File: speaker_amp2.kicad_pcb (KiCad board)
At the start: 2 copper layers, 100 x 85 mm, 74 parts, among them J1 Molex_430450227, J2 Molex_430450227, J3 Molex_430450227, J4 Molex_430450227, J5 Molex_1053101106, J6 Molex_430450227, U1 TAS5822MDCPR, U2 TAS5822MDCPR

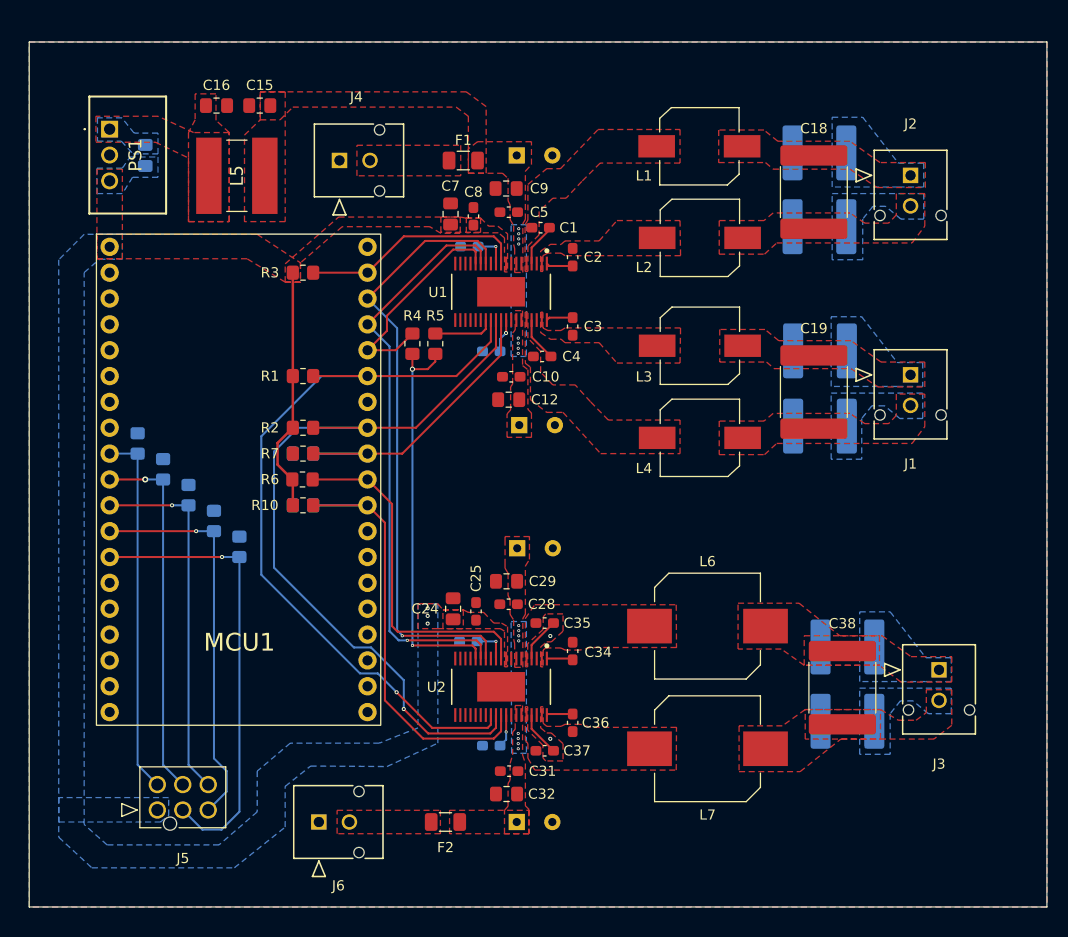
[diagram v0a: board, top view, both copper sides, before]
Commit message: added LEDs and mounting holes
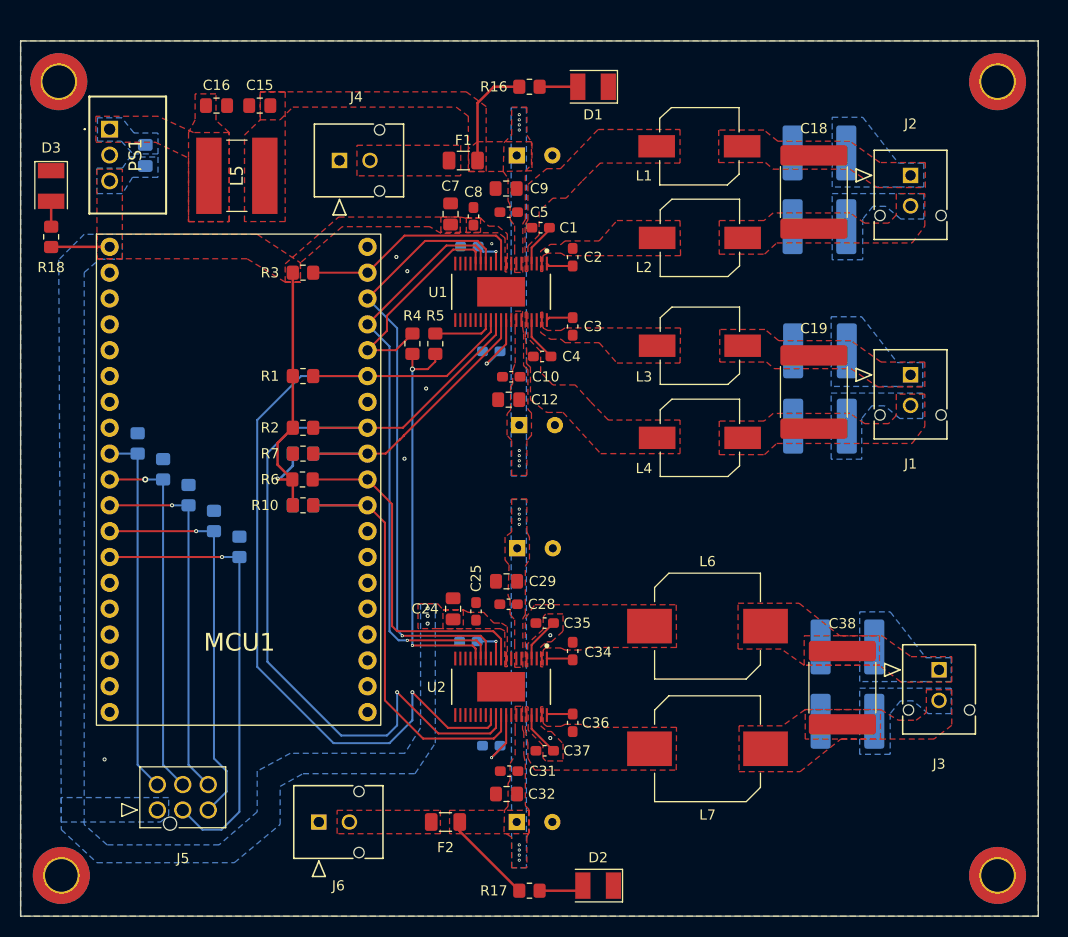
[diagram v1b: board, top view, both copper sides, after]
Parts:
- added D1: Red, LED_SMD:LED_PLCC-2_3.4x3.0mm_KA, F.Cu at (93.8, 69.5)
- added D2: Blue, LED_SMD:LED_PLCC-2_3.4x3.0mm_KA, F.Cu at (94.2, 148.0)
- added D3: Green, LED_SMD:LED_PLCC-2_3.4x3.0mm_KA, F.Cu at (40.5, 79.2)
- added H1: MountingHole_Pad, MountingHole:MountingHole_3.2mm_M3_DIN965_Pad_TopBottom, F.Cu at (41.2, 69.0)
- added H2: MountingHole_Pad, MountingHole:MountingHole_3.2mm_M3_DIN965_Pad_TopBottom, F.Cu at (133.5, 69.0)
- added H3: MountingHole_Pad, MountingHole:MountingHole_3.2mm_M3_DIN965_Pad_TopBottom, F.Cu at (41.5, 147.0)
- added H4: MountingHole_Pad, MountingHole:MountingHole_3.2mm_M3_DIN965_Pad_TopBottom, F.Cu at (133.5, 147.0)
- added R16: 1.6k, Resistor_SMD:R_0805_2012Metric_Pad1.20x1.40mm_HandSolder, F.Cu at (87.5, 69.5)
- added R17: 1.5k, Resistor_SMD:R_0805_2012Metric_Pad1.20x1.40mm_HandSolder, F.Cu at (87.5, 148.5)
- added R18: 120, Resistor_SMD:R_0805_2012Metric_Pad1.20x1.40mm_HandSolder, F.Cu at (40.5, 84.2)
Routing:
- net /SDA: track 77.3 -> 89.6 mm
- net +3.3V: track 24.1 -> 34.6 mm, vias 3 -> 4
- net PVDD: track 0.00 -> 10.4 mm
- net /SCL: track 77.2 -> 86.8 mm
- net PVDD2: track 0.00 -> 9.17 mm
- net Net-(D2-A): track 0.00 -> 4.46 mm
- net Net-(D1-A): track 0.00 -> 3.75 mm
- net Net-(U1-AVDD): track 3.32 -> 6.88 mm
- net Net-(U2-AVDD): track 3.26 -> 6.30 mm
- net Net-(D3-A): track 0.00 -> 2.50 mm
- net /PDN1: track 31.2 -> 30.3 mm
- net GND: vias 2 -> 8
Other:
- board size 100 x 85 mm -> 100 x 86 mm

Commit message: preparing heat vias for amps
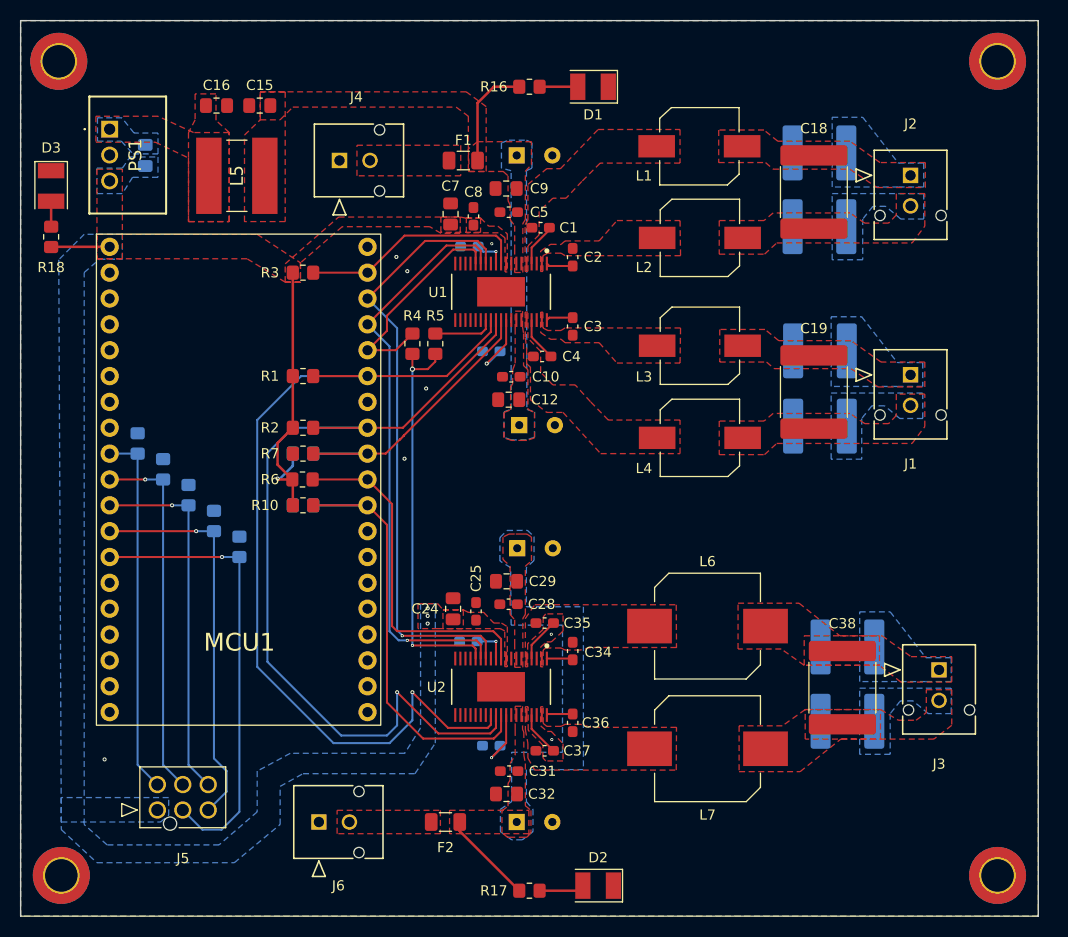
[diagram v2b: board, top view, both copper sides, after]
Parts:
- moved H1 2.00 mm to (41.2, 67.0)
- moved H2 2.00 mm to (133.5, 67.0)
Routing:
- net PVDD2: vias 8 -> 0
- net PVDD: vias 8 -> 0
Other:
- board size 100 x 86 mm -> 100 x 88 mm
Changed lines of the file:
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@@
 	(footprint "MountingHole:MountingHole_3.2mm_M3_DIN965_Pad_TopBottom"
 		(layer "F.Cu")
-		(at 133.5 69)
+		(at 133.5 67)
 		(descr "Mounting Hole 3.2mm, M3, DIN965")
 		(tags "mounting hole 3.2mm m3 din965")
@@
 	(footprint "MountingHole:MountingHole_3.2mm_M3_DIN965_Pad_TopBottom"
 		(layer "F.Cu")
-		(at 41.25 69)
+		(at 41.25 67)
 		(descr "Mounting Hole 3.2mm, M3, DIN965")
 		(tags "mounting hole 3.2mm m3 din965")
@@
 	)
 	(gr_rect
-		(start 37.5 65)
+		(start 37.5 63)
 		(end 137.5 151)
 		(stroke
@@
 	)
 	(via
-		(at 89.55 133.5)
-		(size 0.4)
-		(drill 0.2)
+		(at 89.7 133.65)
+		(size 0.3)
+		(drill 0.15)
 		(layers "F.Cu" "B.Cu")
 		(free yes)
@@
 	)
 	(via
-		(at 89.55 123.4)
-		(size 0.4)
-		(drill 0.2)
+		(at 89.65 123.3)
+		(size 0.3)
+		(drill 0.15)
 		(layers "F.Cu" "B.Cu")
 		(free yes)
@@
 		(net 13)
 	)
-	(via
-		(at 86.5 106.75)
-		(size 0.3)
-		(drill 0.15)
-		(layers "F.Cu" "B.Cu")
-		(free yes)
-		(net 13)
-	)
-	(via
-		(at 86.5 105.25)
-		(size 0.3)
-		(drill 0.15)
-		(layers "F.Cu" "B.Cu")
-		(free yes)
-		(net 13)
-	)
-	(via
-		(at 86.5 106.25)
-		(size 0.3)
-		(drill 0.15)
-		(layers "F.Cu" "B.Cu")
-		(free yes)
-		(net 13)
-	)
-	(via
-		(at 86.5 72.25)
-		(size 0.3)
-		(drill 0.15)
-		(layers "F.Cu" "B.Cu")
-		(free yes)
-		(net 13)
-	)
-	(via
-		(at 86.5 72.75)
-		(size 0.3)
-		(drill 0.15)
-		(layers "F.Cu" "B.Cu")
-		(free yes)
-		(net 13)
-	)
-	(via
-		(at 86.5 105.75)
-		(size 0.3)
-		(drill 0.15)
-		(layers "F.Cu" "B.Cu")
-		(free yes)
-		(net 13)
-	)
-	(via
-		(at 86.5 73.75)
-		(size 0.3)
-		(drill 0.15)
-		(layers "F.Cu" "B.Cu")
-		(free yes)
-		(net 13)
-	)
-	(via
-		(at 86.5 73.25)
-		(size 0.3)
-		(drill 0.15)
-		(layers "F.Cu" "B.Cu")
-		(free yes)
-		(net 13)
-	)
 	(segment
 		(start 85.212499 133.987501)
@@
 	(via
 		(at 49.75 108.09)
-		(size 0.6)
-		(drill 0.3)
+		(size 0.4)
+		(drill 0.2)
 		(layers "F.Cu" "B.Cu")
 		(net 34)
@@
 	)
 	(segment
-		(start 71.59 110.63)
-		(end 73.3 112.34)
+		(start 84.7125 132.8375)
+		(end 84.7125 131.237884)
 		(width 0.2)
 		(layer "F.Cu")
@@
 	)
 	(segment
-		(start 84.7125 132.8375)
-		(end 84.7125 131.237884)
+		(start 73.5 130)
+		(end 77.05 133.55)
 		(width 0.2)
 		(layer "F.Cu")
@@
 	)
 	(segment
-		(start 73.3 129.8)
-		(end 77.05 133.55)
+		(start 73.5 112.54)
+		(end 73.5 130)
 		(width 0.2)
 		(layer "F.Cu")
@@
 	)
 	(segment
-		(start 73.3 112.34)
-		(end 73.3 129.8)
+		(start 71.59 110.63)
+		(end 73.5 112.54)
 		(width 0.2)
 		(layer "F.Cu")
@@
 		(net 89)
 	)
-	(via
-		(at 86.5 111.5)
-		(size 0.3)
-		(drill 0.15)
-		(layers "F.Cu" "B.Cu")
-		(free yes)
-		(net 89)
-	)
-	(via
-		(at 86.5 144.5)
-		(size 0.3)
-		(drill 0.15)
-		(layers "F.Cu" "B.Cu")
-		(free yes)
-		(net 89)
-	)
-	(via
-		(at 86.5 111)
-		(size 0.3)
-		(drill 0.15)
-		(layers "F.Cu" "B.Cu")
-		(free yes)
-		(net 89)
-	)
-	(via
-		(at 86.5 112)
-		(size 0.3)
-		(drill 0.15)
-		(layers "F.Cu" "B.Cu")
-		(free yes)
-		(net 89)
-	)
-	(via
-		(at 86.5 145)
-		(size 0.3)
-		(drill 0.15)
-		(layers "F.Cu" "B.Cu")
-		(free yes)
-		(net 89)
-	)
-	(via
-		(at 86.5 144)
-		(size 0.3)
-		(drill 0.15)
-		(layers "F.Cu" "B.Cu")
-		(free yes)
-		(net 89)
-	)
-	(via
-		(at 86.5 145.5)
-		(size 0.3)
-		(drill 0.15)
-		(layers "F.Cu" "B.Cu")
-		(free yes)
-		(net 89)
-	)
-	(via
-		(at 86.5 112.5)
-		(size 0.3)
-		(drill 0.15)
-		(layers "F.Cu" "B.Cu")
-		(free yes)
-		(net 89)
-	)
 	(segment
 		(start 88.5 69.5)
@@
 			(pts
 				(xy 86.1 132.65) (xy 86.1 130.375) (xy 86.825 130.375) (xy 86.825 132.675) (xy 86.95 132.9) (xy 86.95 135.15)
-				(xy 87.1 136) (xy 87.1 140.15) (xy 87.45 140.5) (xy 87.45 142.75) (xy 87.25 143.25) (xy 87.25 146.25)
-				(xy 85.75 146.25) (xy 85.75 143.25) (xy 85 142.75) (xy 85.05 140.6) (xy 85.4 140.2) (xy 85.4 137.95)
+				(xy 87.1 136) (xy 87.1 140.15) (xy 87.65 140.6) (xy 87.65 142.8) (xy 87.25 143.25) (xy 87.05 143.25)
+				(xy 85.85 143.25) (xy 85.35 143.25) (xy 84.8 142.8) (xy 84.8 140.65) (xy 85.4 140.2) (xy 85.4 137.95)
 				(xy 85.6 137.65) (xy 85.6 136) (xy 86.1 135.175) (xy 86.1 132.925)
 			)
@@
 			(pts
 				(xy 86.05 123.775) (xy 86.05 124.199399) (xy 86.05 126.55) (xy 86.85 126.55) (xy 86.85 121.75) (xy 87.1 121.35)
-				(xy 87.1 116.6) (xy 87.5 115.95) (xy 87.5 113.75) (xy 87.25 113.25) (xy 87.25 110) (xy 85.75 110)
-				(xy 85.75 113.25) (xy 85.1 113.75) (xy 85.1 114.75) (xy 85.1 116) (xy 85.5 116.5) (xy 85.4 119.5)
+				(xy 87.1 116.6) (xy 87.7 116.1) (xy 87.7 113.75) (xy 87.25 113.45) (xy 86.75 113.45) (xy 86.05 113.45)
+				(xy 85.5 113.45) (xy 84.9 113.75) (xy 84.9 114.8) (xy 84.9 115.95) (xy 85.6 116.6) (xy 85.6 119.45)
 				(xy 85.6 119.9) (xy 85.6 121.35) (xy 86.05 121.875)
 			)
@@
 	)
 	(zone
-		(net 13)
-		(net_name "PVDD")
-		(layer "F.Cu")
-		(hatch edge 0.5)
-		(priority 25)
-		(connect_pads yes
-			(clearance 0.25)
-		)
-		(min_thickness 0.2)
-		(filled_areas_thickness no)
-		(fill yes
-			(thermal_gap 0.5)
-			(thermal_bridge_width 0.5)
-			(smoothing fillet)
-			(radius 0.25)
-		)
-		(polygon
-			(pts
-				(xy 84.925 77.825) (xy 85 75) (xy 85.75 74.25) (xy 85.75 71.5) (xy 87.25 71.5) (xy 87.25 74.25)
-				(xy 87.75 75) (xy 87.75 77.75)
-			)
-		)
-	)
-	(zone
 		(net 27)
 		(net_name "Net-(C38-Pad1)")
@@
 				(xy 86.05 85) (xy 86.05 85.399399) (xy 86.05 87.75) (xy 86.85 87.75) (xy 86.85 82.95) (xy 87.1 82.55)
 				(xy 87.1 77.8) (xy 87.7 77.15) (xy 87.7 74.9) (xy 82.4 74.9) (xy 81.5 75.6) (xy 81.575 77.825) (xy 84.925 77.825)
-				(xy 85.4 78.5) (xy 85.4 80.7) (xy 85.6 81.1) (xy 85.6 82.55) (xy 86.05 83.15)
+				(xy 85.4 78.25) (xy 85.4 80.7) (xy 85.6 81.1) (xy 85.6 82.55) (xy 86.05 83.15)
 			)
 		)
@@
 			(pts
 				(xy 86.1 93.4) (xy 86.1 91.55) (xy 86.825 91.55) (xy 86.825 93.1) (xy 86.925 93.75) (xy 86.925 96.9)
-				(xy 87.35 97.3) (xy 87.35 101.2) (xy 87.7 101.55) (xy 87.7 103.75) (xy 87.25 104.25) (xy 87.25 107.7)
-				(xy 85.75 107.7) (xy 85.75 104.25) (xy 85.3 103.75) (xy 85.3 101.65) (xy 85.65 101.25) (xy 85.65 99)
-				(xy 85.85 98.7) (xy 85.85 97.325) (xy 86.1 96.675) (xy 86.1 93.675)
+				(xy 87.35 97.3) (xy 87.35 101.2) (xy 88 101.5) (xy 88 104) (xy 87.25 104.25) (xy 87 104.25) (xy 86 104.25)
+				(xy 85.75 104.25) (xy 85 104) (xy 85 101.5) (xy 85.65 101.25) (xy 85.65 99) (xy 85.85 98.7) (xy 85.85 97.325)
+				(xy 86.1 96.675) (xy 86.1 93.675)
 			)
 		)
@@
 		(polygon
 			(pts
-				(xy 37.5 65) (xy 137.5 65) (xy 137.5 151) (xy 37.5 151)
+				(xy 37.5 63) (xy 137.5 63) (xy 137.5 151) (xy 37.5 151)
 			)
 		)
@@
 		(polygon
 			(pts
-				(xy 85.7 71.55) (xy 87.2 71.55) (xy 87.2 107.75) (xy 85.7 107.75)
+				(xy 85 103.95) (xy 85 101.45) (xy 85.7 101.2) (xy 85.7 77.75) (xy 84.75 77.5) (xy 84.75 75) (xy 85.5 74.75)
+				(xy 87.2 74.75) (xy 87.75 75) (xy 87.75 77.5) (xy 87.205671 77.750084) (xy 87.25 101.2) (xy 88 101.45)
+				(xy 88 103.95) (xy 87.2 104.2) (xy 85.7 104.2)
 			)
 		)
@@
 			(thermal_bridge_width 0.5)
 			(smoothing fillet)
-			(radius 0.25)
+			(radius 0.5)
 		)
 		(polygon
 			(pts
-				(xy 85.7 110.05) (xy 87.2 110.05) (xy 87.2 146.25) (xy 85.75 146.25)
+				(xy 84.65 140.5) (xy 85.75 139.75) (xy 85.75 134.9) (xy 90.75 134.9) (xy 90.75 122.4) (xy 85.7 122.4)
+				(xy 85.65 116.75) (xy 84.6 116.1) (xy 84.6 113.798071) (xy 85.3 113.1) (xy 87.30018 113.091004)
+				(xy 87.95 113.7) (xy 87.95 116.05) (xy 87.2 116.75) (xy 87.2 120.6) (xy 92.8 120.6) (xy 92.8 136.6)
+				(xy 87.2 136.6) (xy 87.2 139.75) (xy 87.85 140.5) (xy 87.85 142.7) (xy 86.8 143.5) (xy 85.75 143.5)
+				(xy 84.65 142.7)
 			)
 		)

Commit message: Added array of thermal reliefs
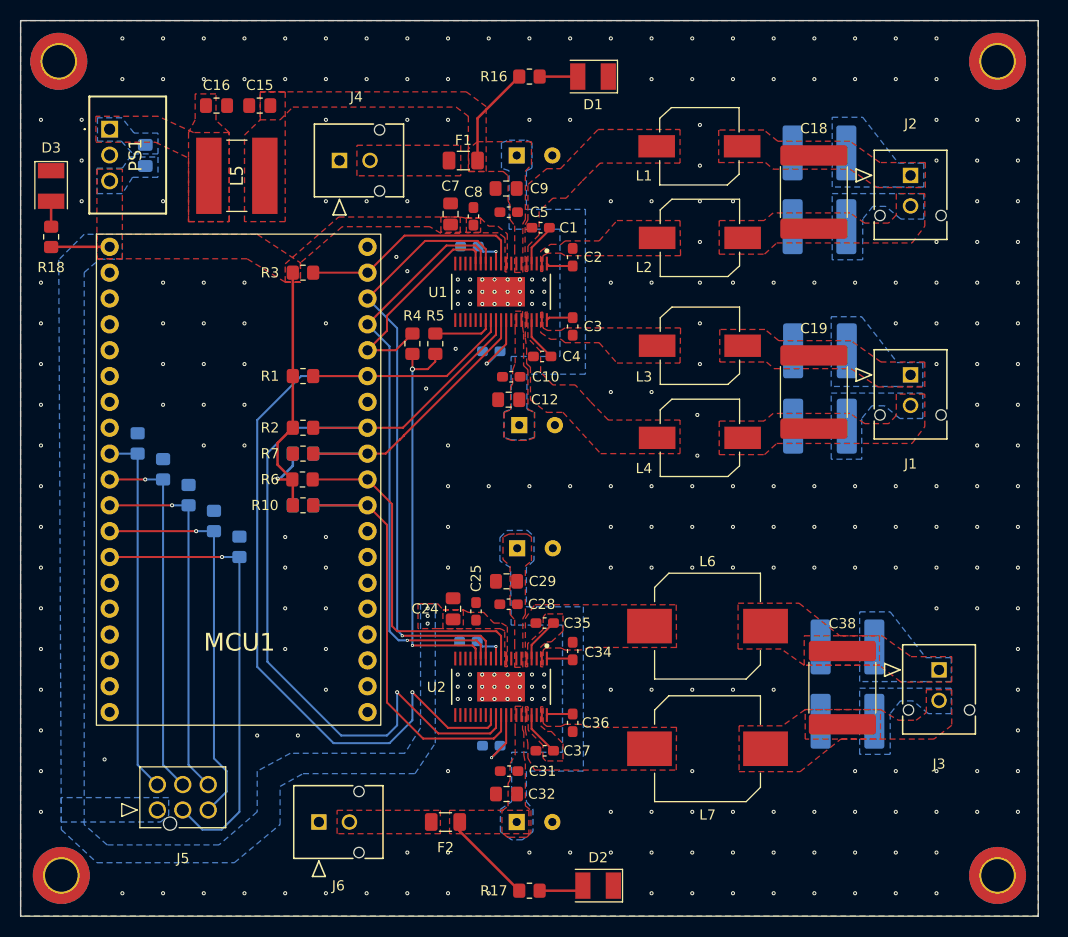
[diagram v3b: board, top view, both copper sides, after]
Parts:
- moved D1 1.00 mm to (93.8, 68.5)
- moved R16 1.00 mm to (87.5, 68.5)
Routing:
- net unconnected-(MCU1-GPIO16-Pad31): vias 0 -> 1
- net Net-(F1-Pad2): vias 0 -> 1
- net GND: vias 8 -> 290
- net /Next: vias 1 -> 2
- net +3.3V: vias 4 -> 5

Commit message: final design + BoM
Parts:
- C38: footprint Speaker Amp Lib:C_2824 -> Capacitor_SMD:C_2220_5750Metric_Pad1.97x5.40mm_HandSolder
- moved C38 0.20 mm to (118.2, 128.8)
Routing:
- net Net-(U2-SDIN): track 39.3 -> 42.3 mm
- net Net-(U2-AVDD): track 6.30 -> 7.12 mm
- net /SCLK: track 57.7 -> 58.3 mm
- net unconnected-(MCU1-GPIO16-Pad31): vias 1 -> 0
- net Net-(F1-Pad2): vias 1 -> 0
- net GND: vias 290 -> 296
- net /Next: vias 2 -> 1
- net +3.3V: vias 5 -> 4

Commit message: final design, sent for production
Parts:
- added G***: LOGO, img:img, B.Cu at (102.8, 105.2)
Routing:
- net /SDA: track 89.6 -> 90.5 mm
- net /ADR2: track 34.1 -> 33.3 mm
- net /SCL: track 86.8 -> 86.1 mm
- net +3.3V: vias 4 -> 3
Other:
- board text added: "BT Speaker Amp v1 - RevB"
- board text added: "Daaaaaamn"
- board text added: "Relasko"
